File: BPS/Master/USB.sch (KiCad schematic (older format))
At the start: 9 parts, among them J20 USBConnector, J21 USB_B_Micro, U17 CP2102N-A01-GQFN24

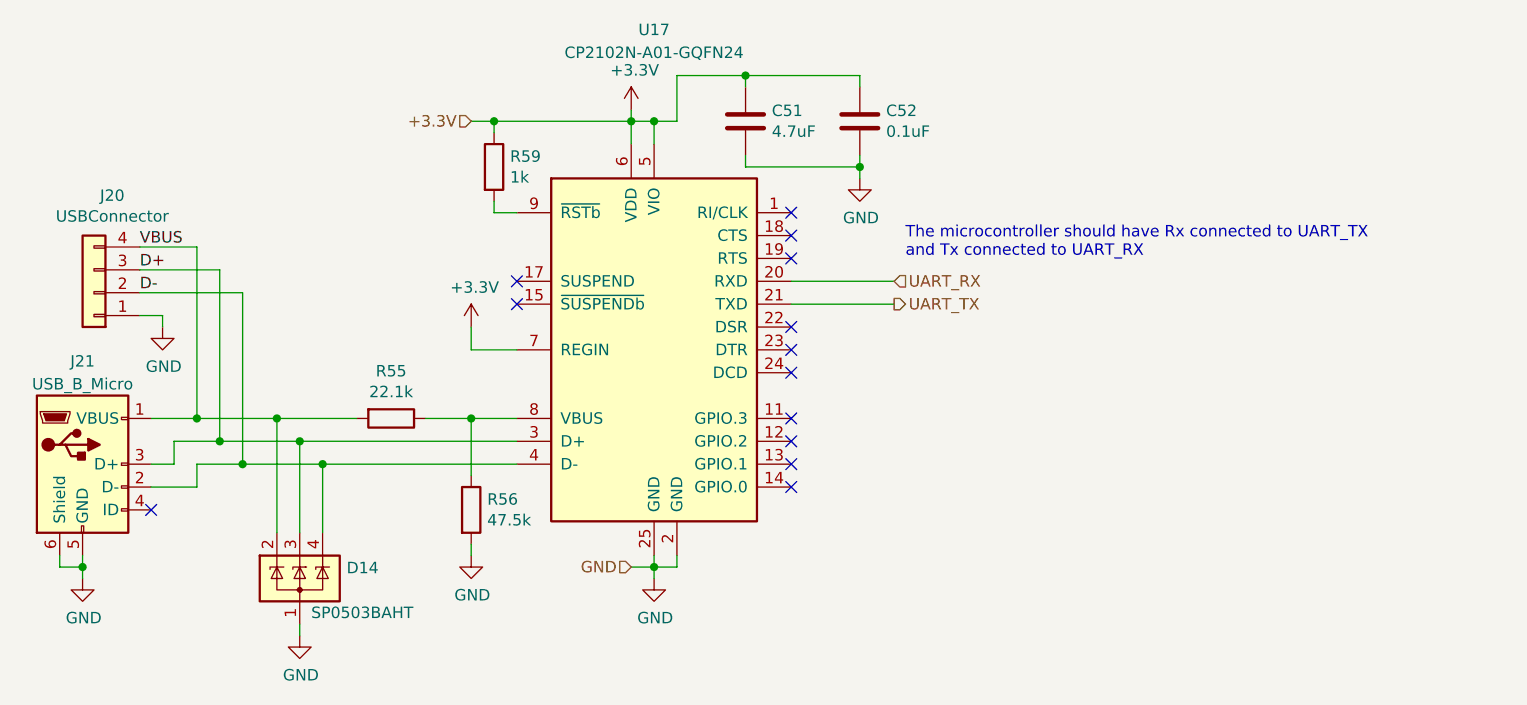
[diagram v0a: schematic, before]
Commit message: Adds master board v1.1.
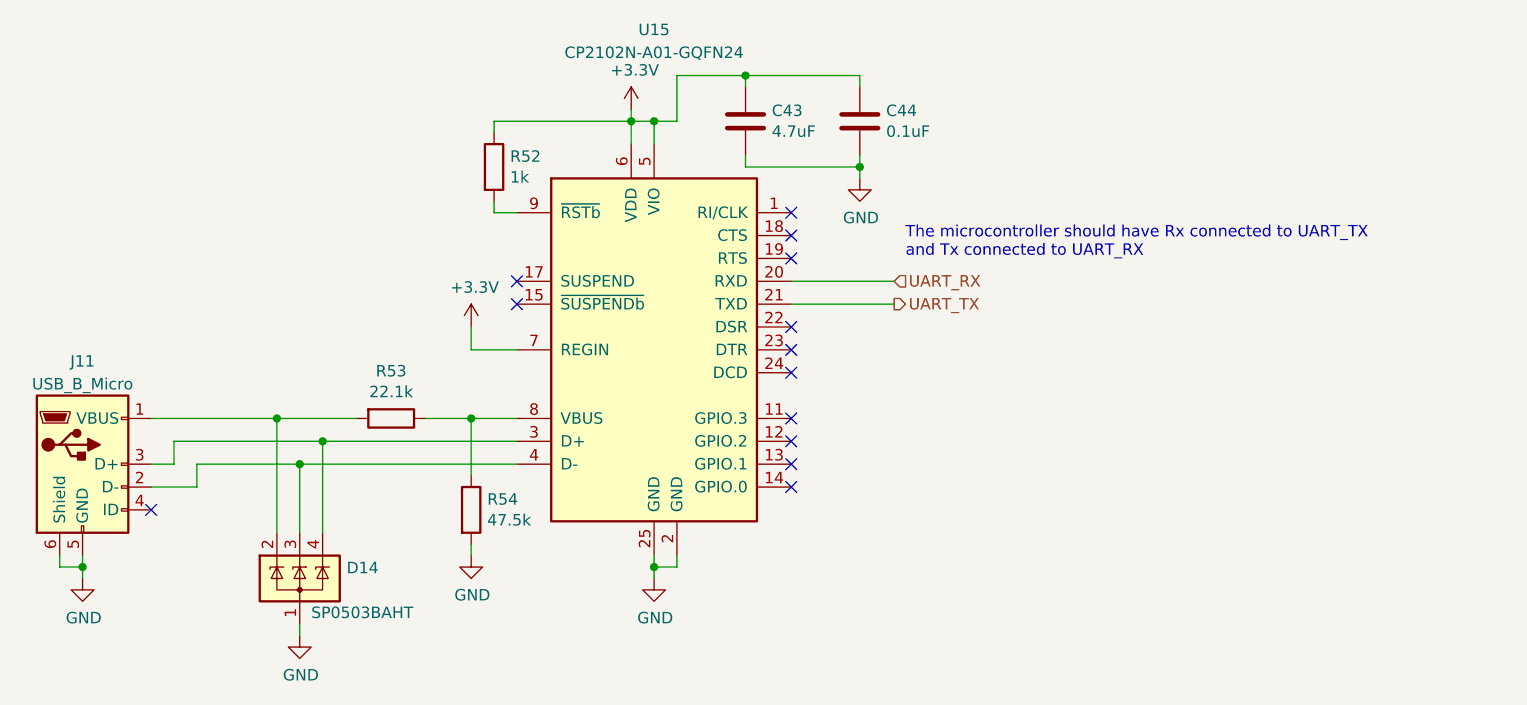
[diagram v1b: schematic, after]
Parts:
- removed J20: USBConnector, UTSVT_Connectors:Molex_MicroFit3.0_1x4xP3.00mm_PolarizingPeg_Vertical, symbol Connector_Generic:Conn_01x04
- renumbered C51 to C43, C52 to C44, J21 to J11, R59 to R52, R55 to R53, R56 to R54, U17 to U15
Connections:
- net D+: no longer names the net of J11.3 (D+), U15.3 (D+)
- net D+: now also D14.4 (K); no longer D14.3 (K)
- net D-: no longer names the net of J11.2 (D-), U15.4 (D-)
- net D-: now also D14.3 (K); no longer D14.4 (K)
- net VBUS: no longer names the net of D14.2 (K), J11.1 (VBUS), R53.2
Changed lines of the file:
@@
 EESchema Schematic File Version 4
 LIBS:BPSMaster-cache
-EELAYER 26 0
+EELAYER 30 0
 EELAYER END
 $Descr A4 11693 8268
 encoding utf-8
-Sheet 8 8
+Sheet 11 11
 Title ""
 Date ""
@@
 $EndDescr
 $Comp
-L Interface_USB:CP2102N-A01-GQFN24 U17
+L Interface_USB:CP2102N-A01-GQFN24 U15
 U 1 1 5C4963B2
 P 5500 3800
-F 0 "U17" H 5500 5200 50  0000 C CNN
+F 0 "U15" H 5500 5200 50  0000 C CNN
 F 1 "CP2102N-A01-GQFN24" H 5500 5100 50  0000 C CNN
 F 2 "Package_DFN_QFN:QFN-24-1EP_4x4mm_P0.5mm_EP2.6x2.6mm" H 5950 3000 50  0001 L CNN
@@
 $EndComp
 $Comp
-L Connector:USB_B_Micro J21
+L Connector:USB_B_Micro J11
 U 1 1 5C4964BB
 P 3000 4300
-F 0 "J21" H 3000 4750 50  0000 C CNN
+F 0 "J11" H 3000 4750 50  0000 C CNN
 F 1 "USB_B_Micro" H 3000 4650 50  0000 C CNN
 F 2 "Connector_USB:USB_Micro-B_Molex-105017-0001" H 3150 4250 50  0001 C CNN
@@
 Wire Wire Line
 	3500 4400 3500 4300
-Wire Wire Line
-	3500 4300 3700 4300
-Wire Wire Line
-	3400 4200 3600 4200
-$Comp
-L power:GND #PWR0129
+$Comp
+L power:GND #PWR087
 U 1 1 5C4965DF
 P 3000 4800
-F 0 "#PWR0129" H 3000 4550 50  0001 C CNN
+F 0 "#PWR087" H 3000 4550 50  0001 C CNN
 F 1 "GND" H 3005 4627 50  0000 C CNN
 F 2 "" H 3000 4800 50  0001 C CNN
@@
 Connection ~ 3000 4750
 $Comp
-L power:GND #PWR0130
+L power:GND #PWR088
 U 1 1 5C4966CF
 P 5500 4800
-F 0 "#PWR0130" H 5500 4550 50  0001 C CNN
+F 0 "#PWR088" H 5500 4550 50  0001 C CNN
 F 1 "GND" H 5505 4627 50  0000 C CNN
 F 2 "" H 5500 4800 50  0001 C CNN
@@
 Wire Wire Line
 	5500 4750 5500 4800
-Text HLabel 5400 4750 0    50   Input ~ 0
-GND
-Wire Wire Line
-	5400 4750 5500 4750
 $Comp
 L Power_Protection:SP0503BAHT D14
@@
 $EndComp
 $Comp
-L power:GND #PWR0131
+L power:GND #PWR089
 U 1 1 5C497074
 P 3950 5050
-F 0 "#PWR0131" H 3950 4800 50  0001 C CNN
+F 0 "#PWR089" H 3950 4800 50  0001 C CNN
 F 1 "GND" H 3955 4877 50  0000 C CNN
 F 2 "" H 3950 5050 50  0001 C CNN
@@
 Wire Wire Line
 	3850 4600 3850 4100
-Wire Wire Line
-	3950 4600 3950 4200
-Connection ~ 3950 4200
-$Comp
-L Device:R R56
+$Comp
+L Device:R R54
 U 1 1 5C497DB9
 P 4700 4500
-F 0 "R56" H 4770 4546 50  0000 L CNN
+F 0 "R54" H 4770 4546 50  0000 L CNN
 F 1 "47.5k" H 4770 4455 50  0000 L CNN
 F 2 "Resistor_SMD:R_0805_2012Metric" V 4630 4500 50  0001 C CNN
@@
 $EndComp
 $Comp
-L Device:R R55
+L Device:R R53
 U 1 1 5C497DDB
 P 4350 4100
-F 0 "R55" V 4143 4100 50  0000 C CNN
+F 0 "R53" V 4143 4100 50  0000 C CNN
 F 1 "22.1k" V 4234 4100 50  0000 C CNN
 F 2 "Resistor_SMD:R_0805_2012Metric" V 4280 4100 50  0001 C CNN
@@
 $EndComp
 Wire Wire Line
-	4050 4600 4050 4300
-Wire Wire Line
 	4200 4100 3850 4100
-Wire Wire Line
-	3950 4200 4900 4200
-Wire Wire Line
-	4050 4300 4900 4300
-Connection ~ 4050 4300
-$Comp
-L power:GND #PWR0128
+$Comp
+L power:GND #PWR086
 U 1 1 5C498DBE
 P 4700 4700
-F 0 "#PWR0128" H 4700 4450 50  0001 C CNN
+F 0 "#PWR086" H 4700 4450 50  0001 C CNN
 F 1 "GND" H 4705 4527 50  0000 C CNN
 F 2 "" H 4700 4700 50  0001 C CNN
@@
 	4700 4700 4700 4650
 $Comp
-L power:+3.3V #PWR0124
+L power:+3.3V #PWR083
 U 1 1 5C499E7D
 P 5400 2750
-F 0 "#PWR0124" H 5400 2600 50  0001 C CNN
+F 0 "#PWR083" H 5400 2600 50  0001 C CNN
 F 1 "+3.3V" H 5415 2923 50  0000 C CNN
 F 2 "" H 5400 2750 50  0001 C CNN
@@
 	5400 2800 5500 2800
 Connection ~ 5400 2800
-Text HLabel 4700 2800 0    50   Input ~ 0
-+3.3V
-Wire Wire Line
-	4700 2800 4800 2800
-$Comp
-L Device:R R59
+$Comp
+L Device:R R52
 U 1 1 5C49B01B
 P 4800 3000
-F 0 "R59" H 4870 3046 50  0000 L CNN
+F 0 "R52" H 4870 3046 50  0000 L CNN
 F 1 "1k" H 4870 2955 50  0000 L CNN
 F 2 "Resistor_SMD:R_0805_2012Metric" V 4730 3000 50  0001 C CNN
@@
 Wire Wire Line
 	4800 2800 4800 2850
-Connection ~ 4800 2800
 Wire Wire Line
 	4800 2800 5400 2800
 $Comp
-L Device:C C51
+L Device:C C43
 U 1 1 5C49CC52
 P 5900 2800
-F 0 "C51" H 6015 2846 50  0000 L CNN
+F 0 "C43" H 6015 2846 50  0000 L CNN
 F 1 "4.7uF" H 6015 2755 50  0000 L CNN
 F 2 "Capacitor_SMD:C_0805_2012Metric" H 5938 2650 50  0001 C CNN
@@
 NoConn ~ 6100 4400
 $Comp
-L power:+3.3V #PWR0127
+L power:+3.3V #PWR085
 U 1 1 5C4A2CBF
 P 4700 3700
-F 0 "#PWR0127" H 4700 3550 50  0001 C CNN
+F 0 "#PWR085" H 4700 3550 50  0001 C CNN
 F 1 "+3.3V" H 4715 3873 50  0000 C CNN
 F 2 "" H 4700 3700 50  0001 C CNN
@@
 	4700 3800 4900 3800
 $Comp
-L Device:C C52
+L Device:C C44
 U 1 1 5C4A4791
 P 6400 2800
-F 0 "C52" H 6515 2846 50  0000 L CNN
+F 0 "C44" H 6515 2846 50  0000 L CNN
 F 1 "0.1uF" H 6515 2755 50  0000 L CNN
 F 2 "Capacitor_SMD:C_0805_2012Metric" H 6438 2650 50  0001 C CNN
@@
 $EndComp
 $Comp
-L power:GND #PWR0125
+L power:GND #PWR084
 U 1 1 5C4A4BE4
 P 6400 3050
-F 0 "#PWR0125" H 6400 2800 50  0001 C CNN
+F 0 "#PWR084" H 6400 2800 50  0001 C CNN
 F 1 "GND" H 6405 2877 50  0000 C CNN
 F 2 "" H 6400 3050 50  0001 C CNN
@@
 Wire Wire Line
 	5900 2600 5600 2600
-$Comp
-L Connector_Generic:Conn_01x04 J20
-U 1 1 5C4A7247
-P 3050 3550
-F 0 "J20" H 2970 3125 50  0000 C CNN
-F 1 "USBConnector" H 2970 3216 50  0000 C CNN
-F 2 "UTSVT_Connectors:Molex_MicroFit3.0_1x4xP3.00mm_PolarizingPeg_Vertical" H 3050 3550 50  0001 C CNN
-F 3 "~" H 3050 3550 50  0001 C CNN
-	1    3050 3550
-	-1   0    0    1
-$EndComp
-$Comp
-L power:GND #PWR0126
-U 1 1 5C4A76D2
-P 3350 3700
-F 0 "#PWR0126" H 3350 3450 50  0001 C CNN
-F 1 "GND" H 3355 3527 50  0000 C CNN
-F 2 "" H 3350 3700 50  0001 C CNN
-F 3 "" H 3350 3700 50  0001 C CNN
-	1    3350 3700
-	1    0    0    -1
-$EndComp
-Wire Wire Line
-	3350 3700 3350 3650
-Wire Wire Line
-	3350 3650 3250 3650
-Wire Wire Line
-	3250 3350 3500 3350
-Wire Wire Line
-	3600 3450 3250 3450
-Wire Wire Line
-	3250 3550 3700 3550
 Connection ~ 4700 4100
 Wire Wire Line
@@
 	4500 4100 4700 4100
 NoConn ~ 3300 4500
-Text Label 3250 3350 0    50   ~ 0
-VBUS
-Text Label 3250 3450 0    50   ~ 0
-D+
-Text Label 3250 3550 0    50   ~ 0
-D-
-Wire Wire Line
-	3300 4100 3500 4100
 Connection ~ 3850 4100
 Wire Wire Line
-	3500 3350 3500 4100
-Connection ~ 3500 4100
-Wire Wire Line
-	3500 4100 3850 4100
-Wire Wire Line
-	3600 3450 3600 4200
-Connection ~ 3600 4200
-Wire Wire Line
-	3600 4200 3950 4200
-Wire Wire Line
-	3700 3550 3700 4300
-Connection ~ 3700 4300
-Wire Wire Line
-	3700 4300 4050 4300
+	3300 4100 3850 4100
+Wire Wire Line
+	3500 4300 3950 4300
+Wire Wire Line
+	3400 4200 4050 4200
+Wire Wire Line
+	4050 4600 4050 4200
+Connection ~ 4050 4200
+Wire Wire Line
+	4050 4200 4900 4200
+Wire Wire Line
+	3950 4600 3950 4300
+Connection ~ 3950 4300
+Wire Wire Line
+	3950 4300 4900 4300
 $EndSCHEMATC
